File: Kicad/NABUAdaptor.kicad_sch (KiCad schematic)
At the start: 22 parts, among them J1 Conn_01x04, J2 DIN-5_180degree, J3 Conn_01x09, J4 Conn_01x05, U1 74LS164, U12 74LS164, U13 74LS164, U14 74LS04, U2 74LS30, U20 74LS164, U21 74LS86, U24 74LS04, U3 74LS27, U4 74LS27

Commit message: Update Kicad schematic - more frame sync reversing
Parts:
- added R47: R, symbol Device:R
- added TP2: TestPoint, symbol Connector:TestPoint
- added U22: 74LS74, symbol 74xx:74LS74
- added U4: 74LS164, symbol 74xx:74HC164
- renumbered U4 to U3
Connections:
- net +5V: now also J4.4 (Pin_4), U4.14 (VCC), U4.2 (DSB)
- net GND: now also J2.2, R47.1, U4.7 (GND)
- net at TP1.1, U1.3 (Q0), U14.1: now also U4.1 (DSA)
- net FPLED_MESSAGE_K: now reaches J4.1 (Pin_1)
- net FPLED_LINK_K: now reaches J4.2 (Pin_2)
- net FPLED_CABLE_K: now reaches J4.3 (Pin_3)
- net at J4.5 (Pin_5): now also R47.2
- net RS422_RX+: now reaches J2.1
- net RS422_TX-: now reaches J2.3
- net RS422_RX-: now reaches J2.4
- net RS422_TX+: now reaches J2.5
- net at U24.12: now also U22.11 (C)
- net at U24.13, U3.12: now also TP2.1, U22.3 (C), U4.8 (CP)
- net PU_R3: now reaches R3.2, U12.9 (~{MR}), U13.9 (~{MR}), U20.9 (~{MR})
- net PU_R2: now reaches R2.2, U1.9 (~{MR})
- net PU_R2: now also U22.10 (~{S}), U22.4 (~{S}), U4.9 (~{MR})
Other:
- note added: "DELAYED DEMOD_CLOCK"
- note added: "MESSAGE LINK CABLE +5V POWER"
- note added: "OFF-BOARD CONNECTORS"
- note added: "PULLUP"
- note added: "SYNC DETECTOR? ... mystery biscuits!"
- note added: "U1.Q[7..0] = 0011_1110"
- note added: "U1.Q[7..0] = 0111_1110"
- note added: "U1.Q[7..0] = xx11_1110"
- note removed: "U1[7..0] = xx11_1110"
- moved on the sheet: C4, Cxx, J1, J2, J3, J4, R2, R3, TP1, U1, U12, U13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

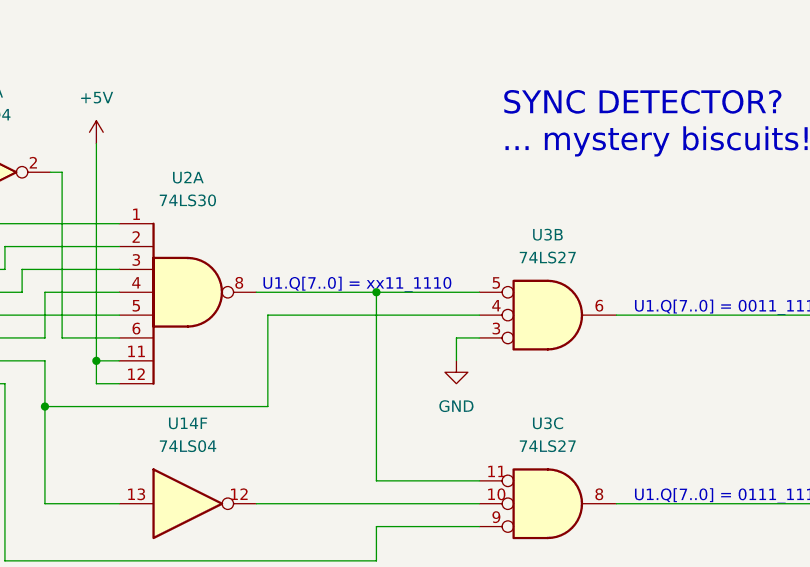
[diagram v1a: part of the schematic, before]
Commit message: kicad: fix polarity of U2a output
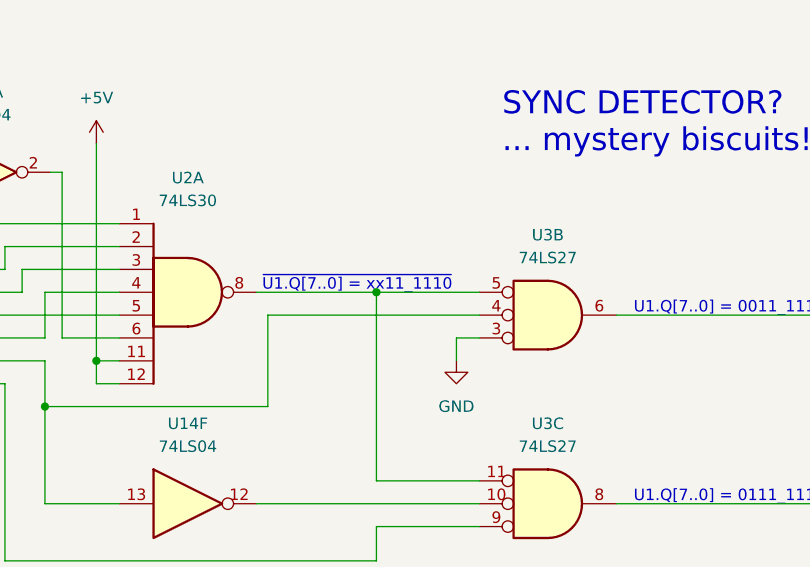
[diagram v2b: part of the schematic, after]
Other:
- note added: "~{U1.Q[7..0] = xx11_1110}"
- note removed: "U1.Q[7..0] = xx11_1110"
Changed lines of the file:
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@@
     (effects (font (size 1.27 1.27)) (justify right bottom))
   )
-  (text "U1.Q[7..0] = xx11_1110" (at 328.93 89.535 0)
+  (text "~{U1.Q[7..0] = xx11_1110}" (at 328.93 89.535 0)
     (effects (font (size 1.27 1.27)) (justify left bottom))
   )

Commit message: kicad: add more U15/U22 wiring
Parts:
- added U15: 74LS74, symbol 74xx:74LS74
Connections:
- net at U22.13 (~{R}): now also U14.10, U15.10 (~{S}), U15.4 (~{S})
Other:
- moved on the sheet: C21, C24, U14E, U21E, U22C, U24G

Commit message: Update schematic - just about done now
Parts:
- added C37, C8: ?VALUE?, symbol Device:C_Polarized
- added C38, C40: ?VALUE?, symbol Device:C
- added CR1, CR2, CR3, CRxxx: 1N4148, symbol Device:D
- added JP1: DNF, symbol Device:R
- added R1, R10, R12, R13, R14, R23, R24, R26, R28, R30, R32, R33, R4, R41, R45, R5, R9, Rxxx_NEAR_R31: 3k3, symbol Device:R
- added R11: 100R, symbol Device:R
- added R15, R17, R18, R19: 1k, symbol Device:R
- added R20, R21, R25: 220k, symbol Device:R
- added R27, R43: 56k, symbol Device:R
- added R29: 12k, symbol Device:R
- added R31: 1k5, symbol Device:R
- added R34: 10Meg, symbol Device:R
- added R35, R36: 560, symbol Device:R
- added R37: 10k, symbol Device:R
- added R38: 10k, symbol Device:R_Potentiometer_Trim
- added R44: 330k, symbol Device:R
- added R46: 220, symbol Device:R
- added R48: 33k, symbol Device:R
- added R7: 56R, symbol Device:R
- added R8: R, symbol Device:R
- added TP3, TP4, TP5, TP6, TP8: TestPoint, symbol Connector:TestPoint
- added U10: UA9638CD, Package_SO:SOIC-8_3.9x4.9mm_P1.27mm, symbol Interface_LineDriver:UA9638CD
- added U11: UA9637, Package_DIP:DIP-8_W7.62mm, symbol Interface_LineDriver:UA9637
- added unit 4 of U14
- added U16: N8X60, symbol 00_NABU-Adapter:N8X60
- added U17, U18: 2114, symbol 00_NABU-Adapter:2114
- added U19: LM339, symbol Comparator:LM339
- added U23, U25, U27: 74LS00, symbol 74xx:74LS00
- added U26, U28, U29, U32: 74LS74, symbol 74xx:74LS74
- added U30: 74LS02, symbol 74xx:74LS02
- added U31: MC6805P2, symbol 00_NABU-Adapter:MC6805P2
- added U33: 74HCU04, symbol 74xx:74HC04
- added U5: PAL16R6 (ID PAL), symbol 00_NABU-Adapter:PAL16R6_NABUAdapter
- added U6: 74LS374, symbol 74xx:74LS374
- added U7: 74LS373, symbol 74xx:74LS373
- added U8: ?VALUE?, Resistor_THT:R_Array_SIP10, symbol Device:R_Network09
- added U9: TR1865PL, symbol 00_NABU-Adapter:TR1865PL
- added Y1: 3.579545MHz, symbol Device:Crystal
- R47: value R -> 240R
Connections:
- net +5V: now also CRxxx.1 (K), R1.2, R10.1, R12.1, R13.1, R14.1, R15.1, R17.1, R19.2, R24.1, R28.1, R30.2, R32.1, R33.1, R37.2, R4.2, R45.2, R48.2, R5.1, R7.1, R9.1, Rxxx_NEAR_R31.1, U10.1 (VCC), U10.1 (VCC), U11.1 (VCC), U11.1 (VCC), U16.13 (LS2), U16.28 (VCC), U17.18 (VCC), U18.18 (VCC), U28.12 (D), U28.2 (D), U31.3 (VCC), U32.2 (D), U5.20 (VCC), U6.20 (VCC), U7.20 (VCC), U8.1 (common), U9.1 (VCC), U9.35 (PI), U9.37 (WLS2), U9.38 (WLS1), U9.39 (EPE)
- net FPLED_CABLE_K: now also R46.2
- net FPLED_LINK_K: now also R36.2
- net FPLED_MESSAGE_K: now also R35.2, R37.1
- net GND: now also U2.7 (GND), U21.7 (GND), U3.7 (GND), C38.2, C40.2, C8.2, CR3.1 (K), JP1.1, R11.1, R18.2, R31.1, R38.3, R41.1, R8.2, U10.4 (GND), U10.4 (GND), U11.4 (GND), U11.4 (GND), U16.12 (LS1), U16.14 (GND), U16.2 (GND), U16.21 (GND), U17.9 (GND), U18.9 (GND), U19.12 (V-), U26.2 (D), U30.5, U30.6, U31.1 (VSS), U31.5 (XTAL), U5.10 (GND), U5.11 (~{OE}), U6.10 (GND), U7.10 (GND), U9.16 (SFD), U9.2 (NC), U9.3 (VSS), U9.36 (SBS)
- net RS422_RX+: now also U11.6 (IN+)
- net RS422_RX-: now also U11.5 (IN-)
- net RS422_TX+: now also U10.6 (OUTB)
- net RS422_TX-: now also U10.5 (OUTA)
- net at U22.1 (~{R}): now also R4.1
- net at U22.2 (D): now also U14.10, U15.10 (~{S}), U15.4 (~{S}), U22.13 (~{R})
- net PAL_P19: now reaches U22.5 (Q)
- net PAL_P19: now also U15.1 (~{R}), U15.13 (~{R}), U23.2, U5.19 (IO19)
- net at U22.6 (~{Q}): now also U26.11 (C)
- net at U22.11 (C), U24.12: now also U15.3 (C)
- net at U22.12 (D): now also U15.11 (C), U15.6 (~{Q})
- net at U22.9 (Q): now also U15.2 (D), U27.10
- net PLL_P2: now reaches J3.2 (Pin_2)
- net PLL_P2: now also R32.2, U31.19 (PB7)
- net PLL_P3: now reaches J3.3 (Pin_3)
- net PLL_P3: now also R43.1
- net PLL_P4: now reaches J3.4 (Pin_4)
- net PLL_P4: now also U11.2 (OUT)
- net PLL_P5: now reaches J3.5 (Pin_5)
- net PLL_P5: now also U10.8 (OUTB)
- net at U15.12 (D): now also U15.8 (~{Q})
- net CABLEDCK_PRE: now reaches U15.9 (Q)
- net CABLEDCK_PRE: now also U14.9, U29.11 (C)
- net CABLEDATA4: now reaches U4.10 (Q4)
- net CABLEDATA4: now also U5.5 (I5), U6.13 (D4)
- net CABLEDATA5: now reaches U4.11 (Q5)
- net CABLEDATA5: now also U5.4 (I4), U6.14 (D5)
- net CABLEDATA6: now reaches U4.12 (Q6)
- net CABLEDATA6: now also U5.3 (I3), U6.17 (D6)
- net CABLEDATA7: now reaches U4.13 (Q7)
- net CABLEDATA7: now also U5.2 (I2), U6.18 (D7)
- net CABLEDATA0: now reaches U4.3 (Q0)
- net CABLEDATA0: now also U5.9 (I9), U6.3 (D0)
- net CABLEDATA1: now reaches U4.4 (Q1)
- net CABLEDATA1: now also U5.8 (I8), U6.4 (D1)
- net CABLEDATA2: now reaches U4.5 (Q2)
- net CABLEDATA2: now also U5.7 (I7), U6.7 (D2)
- net CABLEDATA3: now reaches U4.6 (Q3)
- net CABLEDATA3: now also U5.6 (I6), U6.8 (D3)
- new net: U33.11, U33.12
- new net: R21.1, U33.13
- new net: C38.1, R26.2, R27.1, U19.4 (-)
- new net: R25.2, R26.1, U19.5 (+)
- new net: R13.2, U29.1 (~{R}), U29.13 (~{R})
- new net: R35.1, TP8.1, U31.16 (PB4)
- new net: U23.1, U23.10, U23.6, U23.9
- new net: U23.3, U23.4
- new net: C40.1, R34.1, U33.3, Y1.1
- new net: R34.2, U33.1, U33.4, U33.5, Y1.2
- new net: U28.3 (C), U29.8 (~{Q})
- new net: R17.2, U32.10 (~{S})
- new net: R33.2, U32.12 (D), U32.8 (~{Q}), U9.17 (RRC), U9.40 (TRC)
- new net: R19.1, U32.13 (~{R})
- new net: U29.12 (D), U29.5 (Q)
- new net: C37.1, U33.10, U33.9
- new net: C37.2, R20.2, R21.2
- new net: U16.7 (~{WRITE}), U23.12, U23.13
- new net: R41.2, R43.2, R44.2, U19.9 (+)
- new net: U28.11 (C), U30.13
- new net: TP3.1, U23.8, U27.2
- new net: U26.4 (~{S}), U28.8 (~{Q})
- new net: CR1.1 (K), R23.1
- new net: R44.1, R45.1, R46.1, U19.14
- new net: C8.1, CRxxx.2 (A), R29.2, R30.1, R31.2, U19.11 (+)
- new net: U27.11, U28.10 (~{S})
- new net: R9.2, U26.10 (~{S})
- new net: R7.2, U16.1 (VBB)
- new net: U30.10, U30.2
- new net: R11.2, U16.6 (~{CE})
- new net: U30.1, U9.23 (~{THRL})
- new net: R38.2, U19.8 (-)
- new net: CR2.1 (K), CR3.2 (A)
- new net: CR1.2 (A), Rxxx_NEAR_R31.2
- new net: R38.1, R48.1
- new net: R36.1, U31.17 (PB5)
- new net: U19.1, U19.6 (-)
- new net CABLEDCK: U14.8, U23.5, U27.5, U5.1 (CLK), U6.11 (Cp)
- new net CABLE_FIFO_GATE: U26.9 (Q), U27.1, U27.4
- new net FIFO_WRITE: U23.11, U27.9
- new net F_DQ0: U18.14 (DQ1), U6.2 (O0), U7.3 (D0)
- new net F_DQ1: U18.13 (DQ2), U6.5 (O1), U7.4 (D1)
- new net F_DQ2: U18.12 (DQ3), U6.6 (O2), U7.7 (D2)
- new net F_DQ3: U18.11 (DQ4), U6.9 (O3), U7.8 (D3)
- new net F_DQ4: U17.14 (DQ1), U6.12 (O4), U7.13 (D4)
- new net F_DQ5: U17.13 (DQ2), U6.15 (O5), U7.14 (D5)
- new net F_DQ6: U17.12 (DQ3), U6.16 (O6), U7.17 (D6)
- new net F_DQ7: U17.11 (DQ4), U6.19 (O7), U7.18 (D7)
- new net F_RA0: U16.27 (A0), U17.5 (A0), U18.5 (A0)
- new net F_RA1: U16.26 (A1), U17.6 (A1), U18.6 (A1)
- new net F_RA2: U16.25 (A2), U17.7 (A2), U18.7 (A2)
- new net F_RA3: U16.24 (A3), U17.4 (A3), U18.4 (A3)
- new net F_RA4: U16.23 (A4), U17.3 (A4), U18.3 (A4)
- new net F_RA5: U16.22 (A5), U17.2 (A5), U18.2 (A5)
- new net F_RA6: U16.20 (A6), U17.1 (A6), U18.1 (A6)
- new net F_RA7: U16.19 (A7), U17.17 (A7), U18.17 (A7)
- new net F_RA8: U16.18 (A8), U17.16 (A8), U18.16 (A8)
- new net F_RA9: U16.17 (A9), U17.15 (A9), U18.15 (A9)
- new net MCUD0: U31.20 (PA0), U7.2 (O0), U8.2 (R1), U9.12 (RR1), U9.26 (TR1)
- new net MCUD1: U31.21 (PA1), U7.5 (O1), U8.10 (R9), U9.11 (RR2), U9.27 (TR2)
- new net MCUD2: U31.22 (PA2), U7.6 (O2), U8.9 (R8), U9.10 (RR3), U9.28 (TR3)
- new net MCUD3: U31.23 (PA3), U7.9 (O3), U8.8 (R7), U9.29 (TR4), U9.9 (RR4)
- new net MCUD4: U31.24 (PA4), U7.12 (O4), U8.7 (R6), U9.30 (TR5), U9.8 (RR5)
- new net MCUD5: U31.25 (PA5), U7.15 (O5), U8.6 (R5), U9.31 (TR6), U9.7 (RR6)
- new net MCUD6: U11.8 (IN+), U31.26 (PA6), U7.16 (O6), U8.5 (R4), U9.32 (TR7), U9.6 (RR7)
- new net MCUD7: U10.2 (IN), U31.27 (PA7), U7.19 (O7), U8.4 (R3), U9.33 (TR8), U9.5 (RR8)
- new net MCU_EXTAL: R18.1, U31.4 (EXTAL), U32.11 (C), U33.2, U33.6
- new net MCU_NUM: JP1.2, R15.2, U31.6 (NUM)
- new net MCU_PB0: TP4.1, U31.12 (PB0), U32.3 (C)
- new net MCU_PB2: U30.8, U31.14 (PB2)
- new net MCU_PB6: U30.3, U31.18 (PB6)
- new net MCU_TIMER: R20.1, U31.7 (TIMER), U33.8
- new net PAL_P12: U26.12 (D), U32.5 (Q), U5.12 (IO12)
- new net PAL_P13: U31.10 (PC2), U5.13 (Q13)
- new net PAL_P14: U31.11 (PC3), U5.14 (Q14)
- new net PAL_P17: U26.3 (C), U28.13 (~{R}), U29.3 (C), U5.17 (Q17)
- new net PAL_P18: U28.1 (~{R}), U5.18 (Q18)
- new net PU_R10: R10.2, U26.1 (~{R}), U26.13 (~{R})
- new net PU_R12: R12.2, U28.4 (~{S}), U29.10 (~{S}), U29.4 (~{S}), U32.4 (~{S})
- new net U7_LE: R14.2, TP5.1, U27.12, U28.5 (Q), U29.2 (D), U31.13 (PB1), U7.11 (LE)
- new net UART_DR: U31.8 (PC0), U9.19 (DR)
- new net UART_DRR_RRD: R1.1, U31.15 (PB3), U8.3 (R2), U9.18 (~{DRR}), U9.4 (RRD)
- new net UART_MR: R24.2, R25.1, U19.2, U9.21 (MR)
- new net UART_RI: R23.2, U11.3 (OUT), U9.20 (RI)
- new net UART_THRE: U31.9 (PC1), U9.22 (THRE)
- new net UART_TRO: U10.3 (IN), U9.25 (TRO)
- new net VREF1.4: CR2.2 (A), R5.2, U11.7 (IN-), U19.10 (-)
- new net ~{FIFO_EMPTY}: U16.11 (EMPTY), U27.13, U30.11, U30.12
- new net ~{FIFO_READ}: U16.8 (~{READ}), U30.9
- new net ~{FIFO_RESET}: U16.5 (~{RESET}), U27.3
- new net ~{FIFO_SI}: U16.3 (~{SI}), U27.6
- new net ~{FIFO_SO}: U16.4 (~{SO}), U28.6 (~{Q})
- new net ~{F_CS}: R8.1, U17.8 (~{CS}), U18.8 (~{CS})
- new net ~{F_RAMWE}: U17.10 (~{WE}), U18.10 (~{WE}), U27.8, U6.1 (OE)
- new net ~{MCU_INT}: TP6.1, U26.6 (~{Q}), U31.2 (~{INT}), U32.1 (~{R})
- new net ~{MCU_RST}: R27.2, R28.2, R29.1, U19.13, U31.28 (~{RESET})
- new net ~{U7_OE}: U7.1 (OE)
- no-connect marks 0 -> 3
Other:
- note added: "(Q)"
- note added: "(RESET)"
- note added: "(SET)"
- note added: "1.4V REFERENCE"
- note added: "1.7897725 MHz UART TX/RX CLK"
- note added: "ADDRESS DETECTOR PAL"
- note added: "BYTE RX SHIFTER"
- note added: "CLOCK OSCILLATOR"
- note added: "FIFO DATA TRANSFER LATCHES"
- note added: "FIFO RAM AND CONTROLLER"
- note added: "LS2:1 = 10 = 1024 bytes RAM 512 half length"
- note added: "MCU INTERRUPT GENERATION"
- note added: "MCU TIMER ??? PULSE GENERATOR ???"
- note added: "POWER-ON RESET"
- note added: "RS422 COMMS PORT TX/RX"
- note added: "RSSI THRESHOLD DETECT"
- note added: "SYNC DETECTOR?"
- note added: "UART -> NABU PC"
- note added: "UART CLOCK DIVIDER"
- note removed: "SYNC DETECTOR? ... mystery biscuits!"
- moved on the sheet: C2, C21, C24, C4, Cxx, J1, J2, J3, J4, R2, R3, R47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
